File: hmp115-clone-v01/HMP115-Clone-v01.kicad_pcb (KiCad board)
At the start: 2 copper layers, 85 x 22 mm, 0 parts

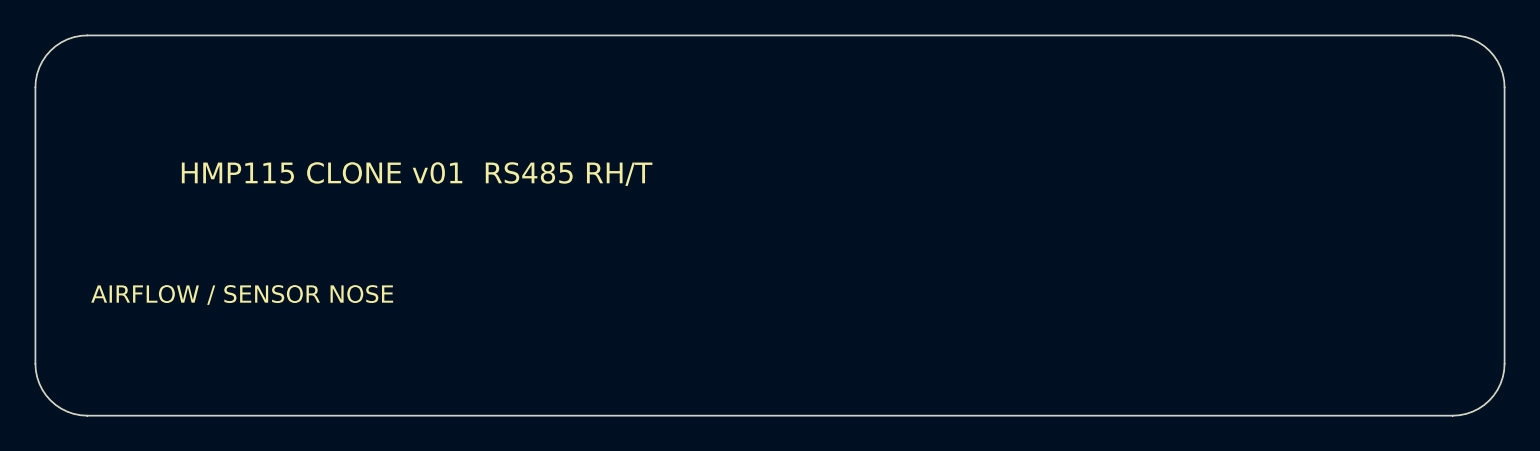
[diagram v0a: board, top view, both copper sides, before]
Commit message: Build routed HMP115 clone v01 prototype
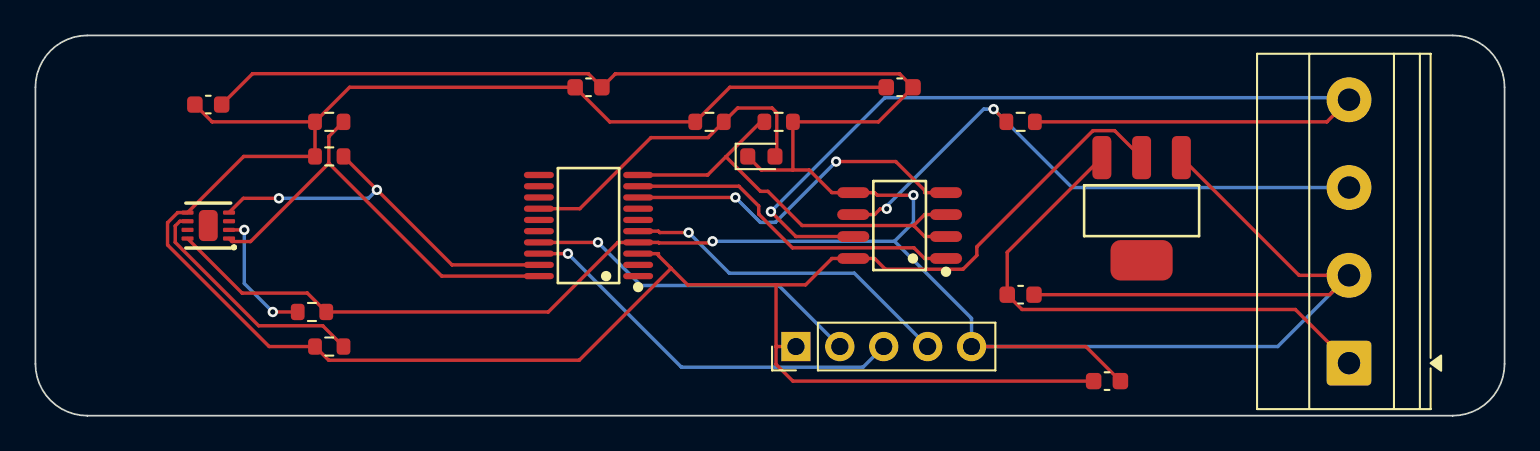
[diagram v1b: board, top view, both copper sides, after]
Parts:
- added C1: 10uF VIN, Capacitor_SMD:C_0603_1608Metric, F.Cu at (57.0, 15.0)
- added C2: 10uF 3V3, Capacitor_SMD:C_0603_1608Metric, F.Cu at (62.0, 20.0)
- added C3: 100nF MCU, Capacitor_SMD:C_0603_1608Metric, F.Cu at (32.0, 3.00)
- added C4: 100nF SHT31, Capacitor_SMD:C_0603_1608Metric, F.Cu at (10.0, 4.00)
- added C5: 100nF RS485, Capacitor_SMD:C_0603_1608Metric, F.Cu at (50.0, 3.00)
- added D1: STATUS, LED_SMD:LED_0603_1608Metric, F.Cu at (42.0, 7.00)
- added J1: FIELD_5-28V_RS485, TerminalBlock_Phoenix:TerminalBlock_Phoenix_MKDS-1,5-4-5.08_1x04_P5.08mm_Horizontal, F.Cu at (76.0, 19.0)
- added J2: SWD_PROG, Connector_PinHeader_2.54mm:PinHeader_1x05_P2.54mm_Vertical, F.Cu at (44.0, 18.0)
- added R1: 4.7k SDA PU, Resistor_SMD:R_0603_1608Metric, F.Cu at (17.0, 5.00)
- added R2: 4.7k SCL PU, Resistor_SMD:R_0603_1608Metric, F.Cu at (17.0, 7.00)
- added R3: 120R TERM DNP, Resistor_SMD:R_0603_1608Metric, F.Cu at (57.0, 5.00)
- added R4: 10k DIR PD, Resistor_SMD:R_0603_1608Metric, F.Cu at (43.0, 5.00)
- added R5: 10k ADDR GND, Resistor_SMD:R_0603_1608Metric, F.Cu at (16.0, 16.0)
- added R6: 1k LED, Resistor_SMD:R_0603_1608Metric, F.Cu at (39.0, 5.00)
- added R7: 10k SHT_RESET PU, Resistor_SMD:R_0603_1608Metric, F.Cu at (17.0, 18.0)
- added U1: STM32C011F6P6, JLC-MCP:TSSOP-20_L6.5-W4.4-P0.65-LS6.4-BL, F.Cu at (32.0, 11.0)
- added U2: SHT31-DIS-B, JLC-MCP:DFN-8_L2.5-W2.5-P0.50-BL-EP, F.Cu at (10.0, 11.0)
- added U3: MAX3485ED, JLC-MCP:SOP-8_L4.9-W3.9-P1.27-LS6.0-BL, F.Cu at (50.0, 11.0)
- added U4: AMS1117-3.3, JLC-MCP:SOT-223-3_L6.5-W3.4-P2.30-LS7.0-BR, F.Cu at (64.0, 10.0)
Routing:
- net GND: track 0.00 -> 182.4 mm, vias 0 -> 2
- net 3V3: track 0.00 -> 150.0 mm
- net RS485_B: track 0.00 -> 60.3 mm, vias 0 -> 1
- net RS485_A: track 0.00 -> 34.2 mm, vias 0 -> 2
- net VIN_5_28V: track 0.00 -> 31.6 mm
- net RS485_DIR: track 0.00 -> 25.4 mm
- net I2C_SDA: track 0.00 -> 25.3 mm
- net SWCLK: track 0.00 -> 23.2 mm, vias 0 -> 1
- net I2C_SCL: track 0.00 -> 23.0 mm, vias 0 -> 2
- net RS485_DI: track 0.00 -> 20.7 mm, vias 0 -> 2
- net SWDIO: track 0.00 -> 19.9 mm, vias 0 -> 1
- net RS485_RO: track 0.00 -> 19.8 mm
- net NRST: track 0.00 -> 19.5 mm, vias 0 -> 1
- net LED_DRV: track 0.00 -> 18.9 mm
- net SHT_RESET: track 0.00 -> 14.0 mm
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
